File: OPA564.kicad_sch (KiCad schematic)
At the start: 0 parts

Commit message: finished adding all footprints i think
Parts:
- added C1, C11, C4, C6, C7, C9: 0.1 uF, Capacitor_SMD:C_0805_2012Metric_Pad1.18x1.45mm_HandSolder, symbol Device:C
- added C10, C12, C2, C3, C5, C8: 47 uF, Capacitor_SMD:C_1210_3225Metric_Pad1.33x2.70mm_HandSolder, symbol Device:C
- added J1, J2, J4, J5, J6: Conn_Coaxial, 731000154:731000154, symbol Connector:Conn_Coaxial
- added R1, R6, R7: 14.2 kOhms, Resistor_SMD:R_0805_2012Metric_Pad1.20x1.40mm_HandSolder, symbol Device:R_US
- added R2, R3, R4, R5: 1 kOhms, Resistor_SMD:R_0805_2012Metric_Pad1.20x1.40mm_HandSolder, symbol Device:R_US
- added U1, U2, U3: OPA564AIDWPR, OPA564AIDWP:SOIC127P1040X265-21N, symbol 2026-05-25_22-15-10:OPA564AIDWPR
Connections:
- new net: J4.1 (In), U2.15 (VOUT), U2.16 (VOUT), U2.6 (-IN)
- new net: J5.1 (In), R2.2, R3.1, U1.15 (VOUT), U1.16 (VOUT), U2.5 (+IN)
- new net: R6.1, U2.9 (ISET)
- new net: J6.1 (In), R4.2, R5.1, U3.15 (VOUT), U3.16 (VOUT)
- new net: J2.1 (In), U3.5 (+IN)
- new net: R4.1, U3.6 (-IN)
- new net: R7.1, U3.9 (ISET)
- new net: R1.1, U1.9 (ISET)
- new net: J1.1 (In), U1.5 (+IN)
- new net: R2.1, U1.6 (-IN)
- new net +12V: C1.2, C10.2, C2.2, C5.2, C6.2, C9.2, U1.17 (V+PWR), U1.18 (V+PWR), U1.19 (V+PWR), U1.2 (V+), U2.17 (V+PWR), U2.18 (V+PWR), U2.19 (V+PWR), U2.2 (V+), U3.17 (V+PWR), U3.18 (V+PWR), U3.19 (V+PWR), U3.2 (V+)
- new net -12V: C11.1, C12.1, C3.1, C4.1, C7.1, C8.1, R1.2, R6.2, R7.2, U1.1 (V-), U1.10 (V-), U1.11 (V-), U1.13 (V-PWR), U1.14 (V-PWR), U1.20 (V-), U1.21 (EP), U2.1 (V-), U2.10 (V-), U2.11 (V-), U2.13 (V-PWR), U2.14 (V-PWR), U2.20 (V-), U2.21 (EP), U3.1 (V-), U3.10 (V-), U3.11 (V-), U3.13 (V-PWR), U3.14 (V-PWR), U3.20 (V-), U3.21 (EP)
- new net -8V: U1.7 (VDIG), U2.7 (VDIG), U3.7 (VDIG)
- new net GND: C1.1, C10.1, C11.2, C12.2, C2.1, C3.2, C4.2, C5.1, C6.1, C7.2, C8.2, C9.1, J1.2 (Ext), J2.2 (Ext), J4.2 (Ext), J5.2 (Ext), J6.2 (Ext), R3.2, R5.2
- no-connect marks 0 -> 12
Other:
- title: (none) -> OPA564 Function Amplifier

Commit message: Rough Sketch of PCB design has been finished
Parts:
- removed J2, J5: Conn_Coaxial, 731000154:731000154, symbol Connector:Conn_Coaxial
- added J7: V-, bidpl:banana_cinch, symbol Connector:Conn_01x01_Socket
- added J8: V+, bidpl:banana_cinch, symbol Connector:Conn_01x01_Socket
- added J9: GND, bidpl:banana_cinch, symbol Connector:Conn_01x01_Socket
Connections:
- net Signal Input: now reaches U3.5 (+IN)
- net Signal Input: now also J1.1 (In), U1.5 (+IN)
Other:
- moved on the sheet: J1

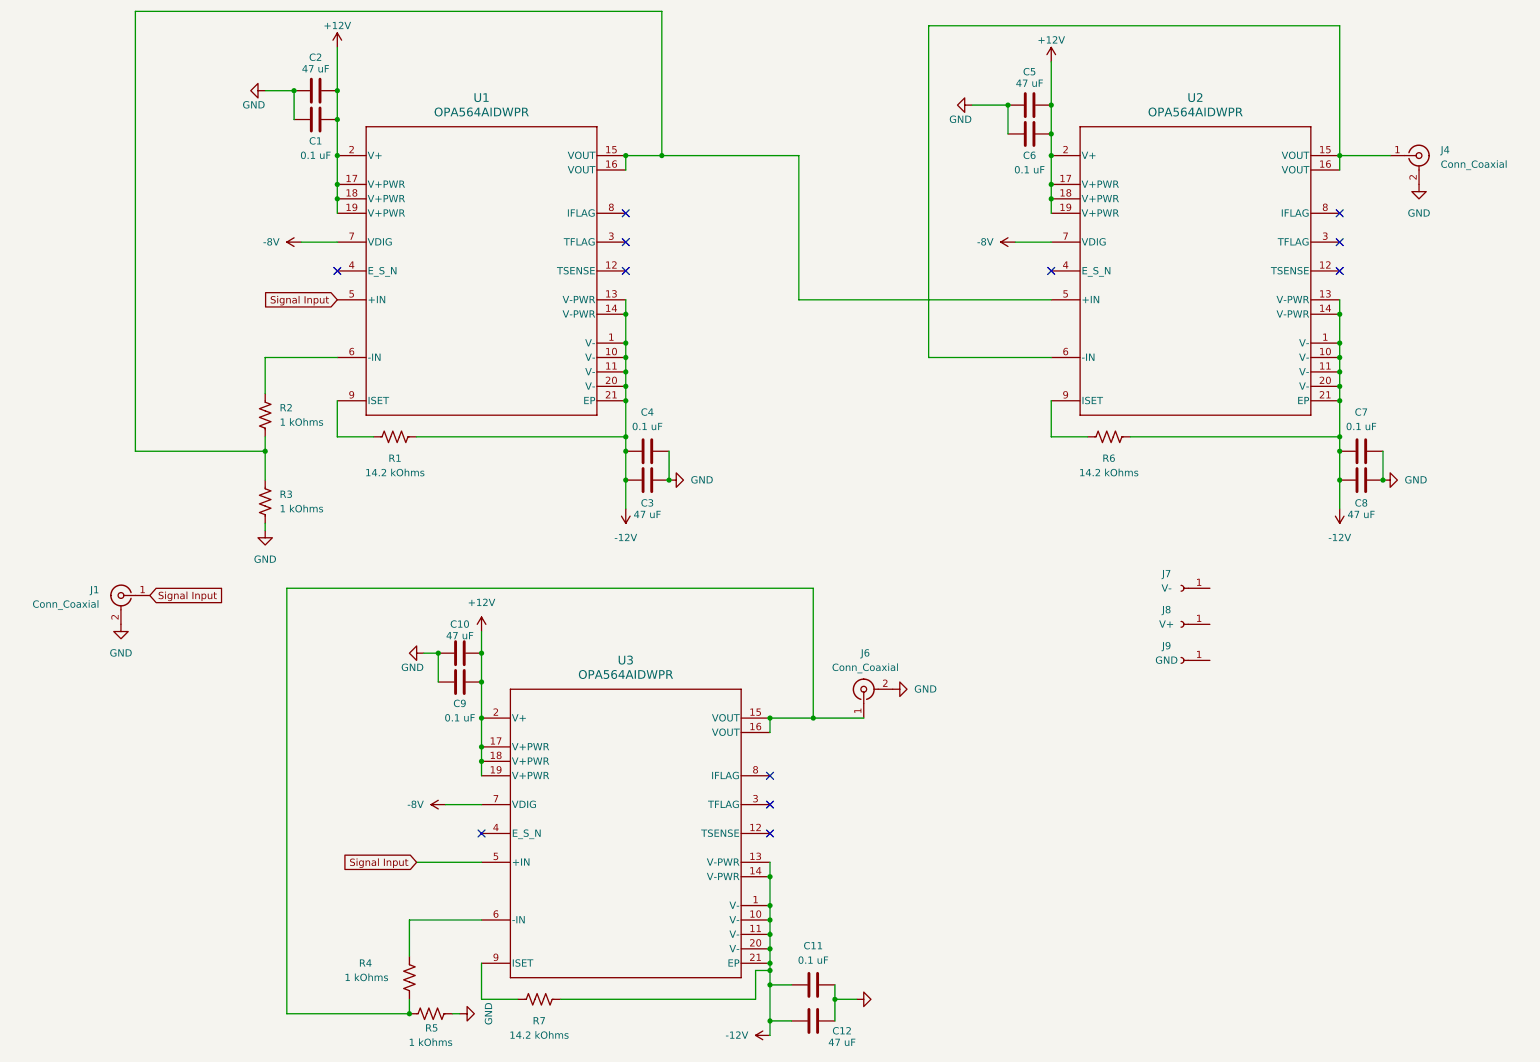
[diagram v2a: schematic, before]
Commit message: OPA564 without Voltage Follower
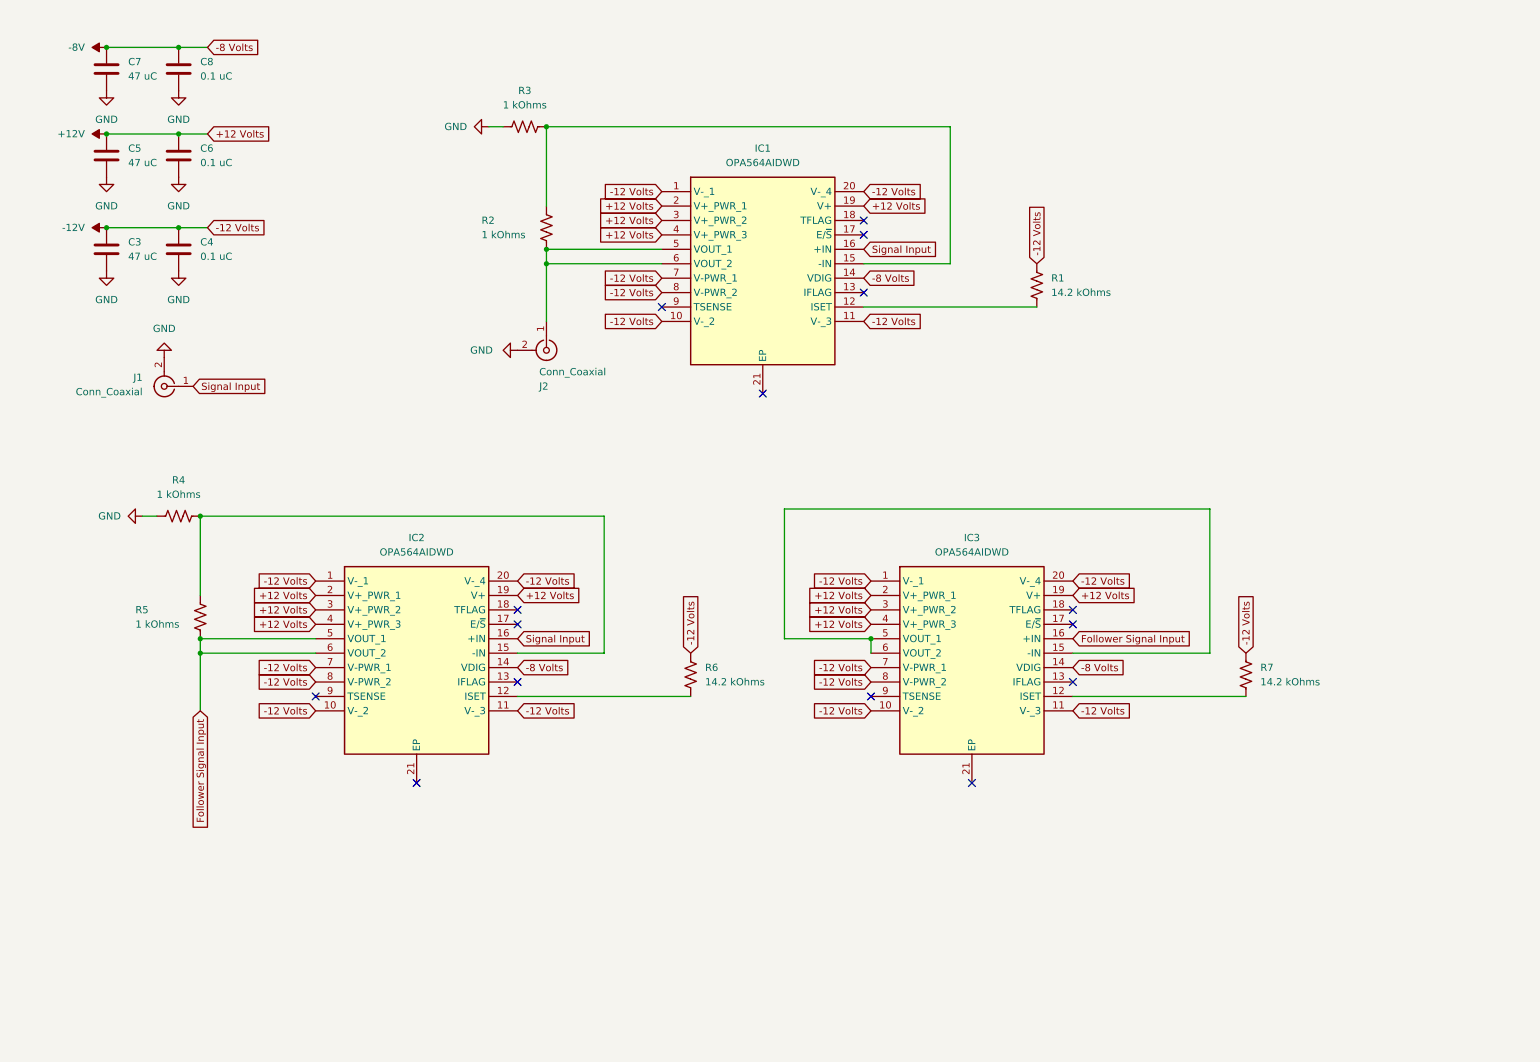
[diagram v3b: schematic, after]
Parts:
- removed C1, C11, C9: 0.1 uF, Capacitor_SMD:C_0805_2012Metric_Pad1.18x1.45mm_HandSolder, symbol Device:C
- removed C10, C12, C2: 47 uF, Capacitor_SMD:C_1210_3225Metric_Pad1.33x2.70mm_HandSolder, symbol Device:C
- removed J4, J6: Conn_Coaxial, 731000154:731000154, symbol Connector:Conn_Coaxial
- removed J7: V-, bidpl:banana_cinch, symbol Connector:Conn_01x01_Socket
- removed J8: V+, bidpl:banana_cinch, symbol Connector:Conn_01x01_Socket
- removed J9: GND, bidpl:banana_cinch, symbol Connector:Conn_01x01_Socket
- removed U1, U2, U3: OPA564AIDWPR, OPA564AIDWP:SOIC127P1040X265-21N, symbol 2026-05-25_22-15-10:OPA564AIDWPR
- added IC1, IC2, IC3: OPA564AIDWD, OPA564AIDWP:SOIC127P1040X265-21N, symbol OPA564AIDWD:OPA564AIDWD
- added J2: Conn_Coaxial, 731000154:731000154, symbol Connector:Conn_Coaxial
- C3, C5: value 47 uF -> 47 uC; footprint Capacitor_SMD:C_1210_3225Metric_Pad1.33x2.70mm_HandSolder -> Capacitor_SMD:C_1812_4532Metric_Pad1.57x3.40mm_HandSolder
- C4, C6: value 0.1 uF -> 0.1 uC
- C7: value 0.1 uF -> 47 uC; footprint Capacitor_SMD:C_0805_2012Metric_Pad1.18x1.45mm_HandSolder -> Capacitor_SMD:C_1812_4532Metric_Pad1.57x3.40mm_HandSolder
- C8: value 47 uF -> 0.1 uC; footprint Capacitor_SMD:C_1210_3225Metric_Pad1.33x2.70mm_HandSolder -> Capacitor_SMD:C_0805_2012Metric_Pad1.18x1.45mm_HandSolder
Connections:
- net +12V: now also IC1.19 (V+), IC1.2 (V+_PWR_1), IC1.3 (V+_PWR_2), IC1.4 (V+_PWR_3), IC2.19 (V+), IC2.2 (V+_PWR_1), IC2.3 (V+_PWR_2), IC2.4 (V+_PWR_3), IC3.19 (V+), IC3.2 (V+_PWR_1), IC3.3 (V+_PWR_2), IC3.4 (V+_PWR_3)
- net -12V: now also C3.2, C4.2, R1.1, R6.1, R7.1, IC1.1 (V-_1), IC1.10 (V-_2), IC1.11 (V-_3), IC1.20 (V-_4), IC1.7 (V-PWR_1), IC1.8 (V-PWR_2), IC2.1 (V-_1), IC2.10 (V-_2), IC2.11 (V-_3), IC2.20 (V-_4), IC2.7 (V-PWR_1), IC2.8 (V-PWR_2), IC3.1 (V-_1), IC3.10 (V-_2), IC3.11 (V-_3), IC3.20 (V-_4), IC3.7 (V-PWR_1), IC3.8 (V-PWR_2); no longer C3.1, C4.1, C7.1, C8.1, R1.2, R6.2, R7.2
- net -8V: now also C7.2, C8.2, IC1.14 (VDIG), IC2.14 (VDIG), IC3.14 (VDIG)
- net GND: now also C3.1, C4.1, C7.1, C8.1, R3.1, R4.1, J2.2 (Ext); no longer C3.2, C4.2, C7.2, C8.2, R3.2, R5.2
- net Signal Input: now also IC1.16 (+IN), IC2.16 (+IN)
- net at R2.2: now also IC1.5 (VOUT_1), IC1.6 (VOUT_2), J2.1 (In); no longer R3.1
- net at R4.2, R5.1: now also IC2.15 (-IN)
- net at R2.1: now also R3.2, IC1.15 (-IN)
- new net: IC3.12 (ISET), R7.2
- new net: IC3.15 (-IN), IC3.5 (VOUT_1), IC3.6 (VOUT_2)
- new net: IC1.12 (ISET), R1.2
- new net: IC2.12 (ISET), R6.2
- new net Follower Signal Input: IC2.5 (VOUT_1), IC2.6 (VOUT_2), IC3.16 (+IN), R5.2
- no-connect marks 12 -> 15

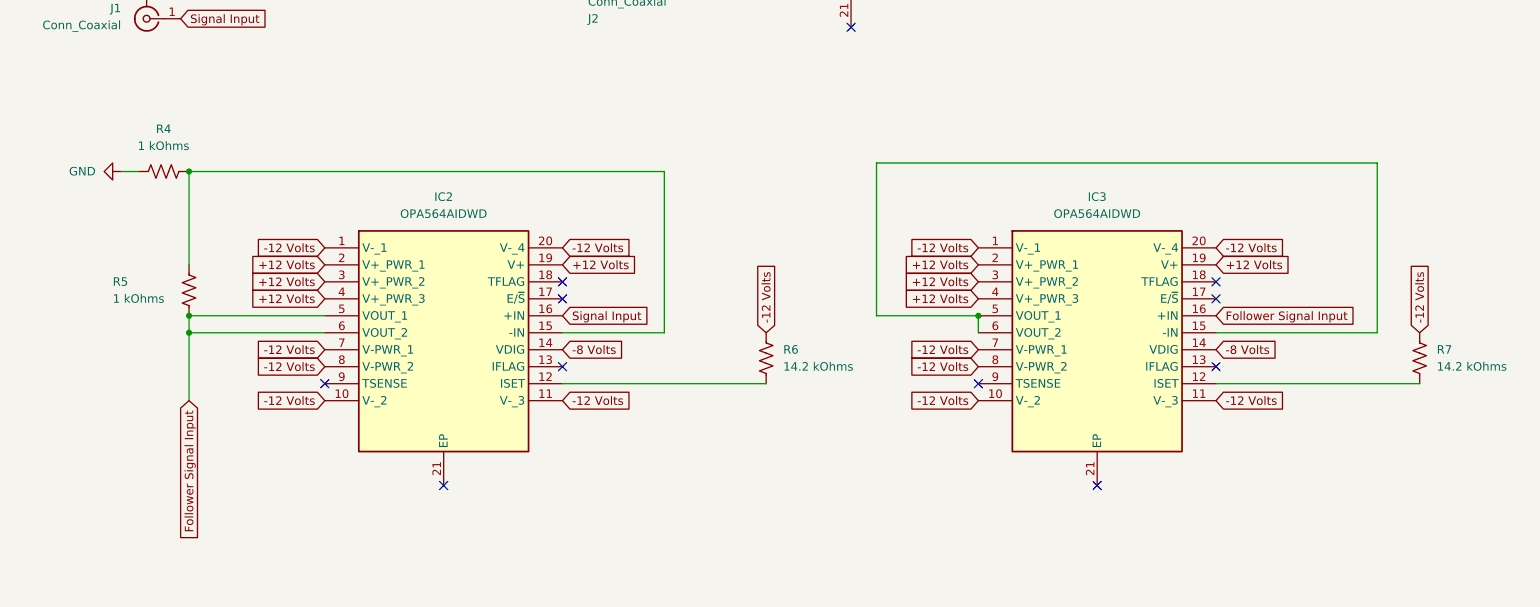
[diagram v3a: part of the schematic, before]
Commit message: OPA564 without voltage follower
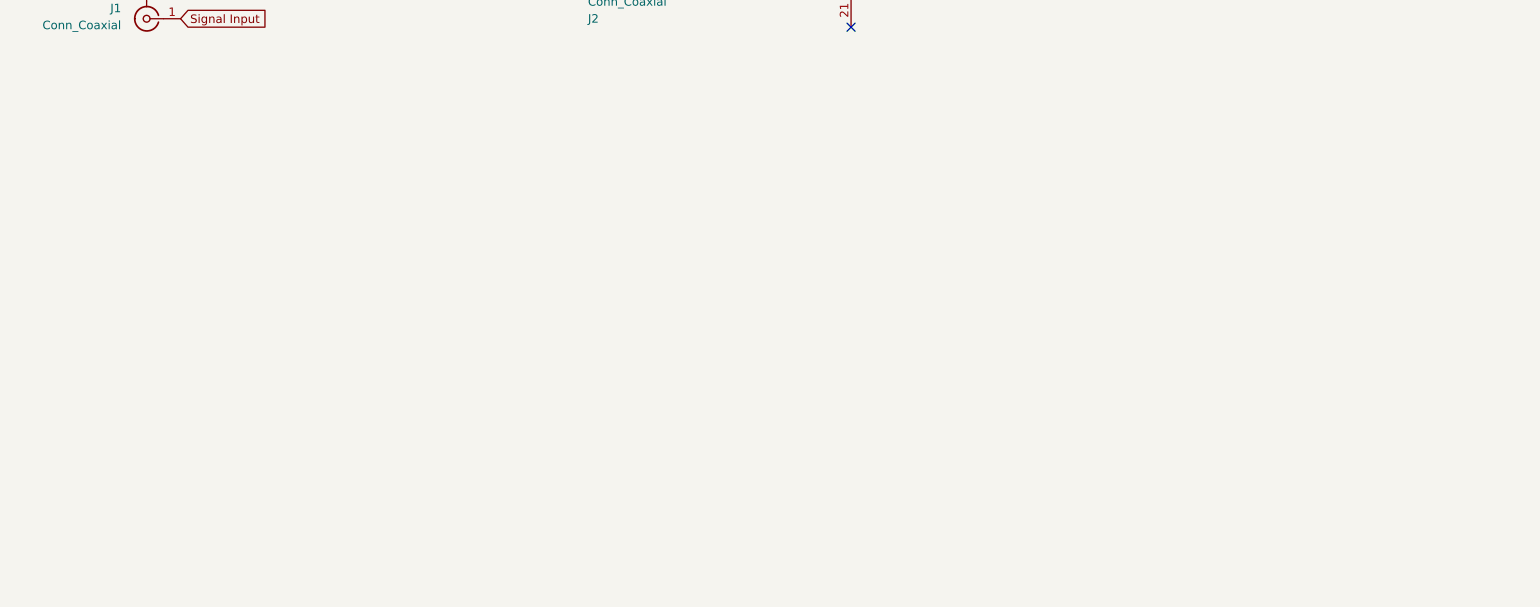
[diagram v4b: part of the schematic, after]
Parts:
- removed IC2, IC3: OPA564AIDWD, OPA564AIDWP:SOIC127P1040X265-21N, symbol OPA564AIDWD:OPA564AIDWD
- removed R4, R5: 1 kOhms, Resistor_SMD:R_0805_2012Metric_Pad1.20x1.40mm_HandSolder, symbol Device:R_US
- removed R6, R7: 14.2 kOhms, Resistor_SMD:R_0805_2012Metric_Pad1.20x1.40mm_HandSolder, symbol Device:R_US
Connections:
- no-connect marks 15 -> 5

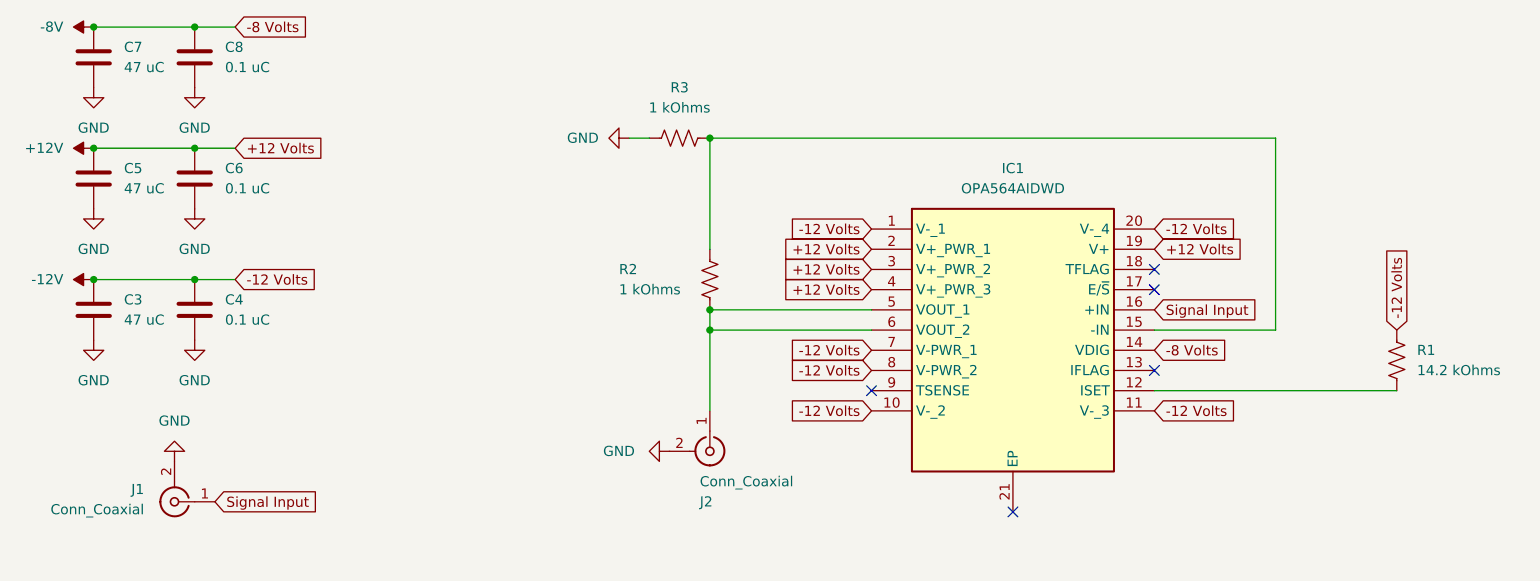
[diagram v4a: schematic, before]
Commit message: OPA564 simplest design
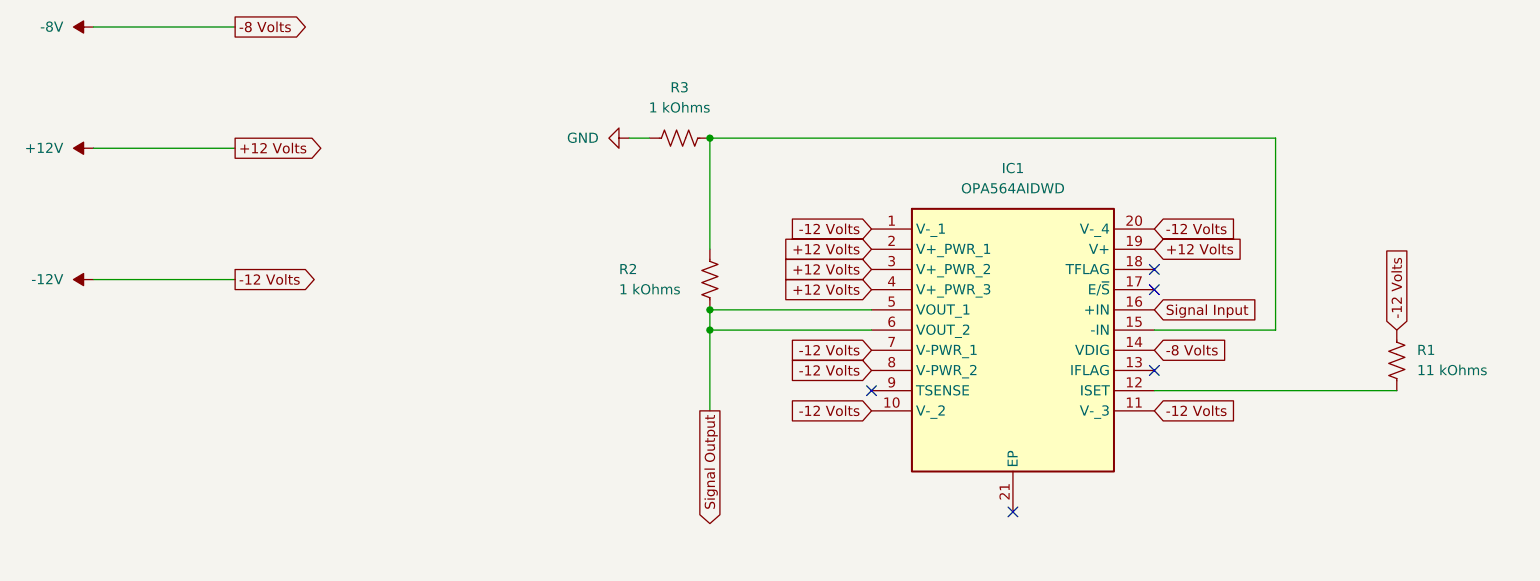
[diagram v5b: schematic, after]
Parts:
- removed C3, C5, C7: 47 uC, Capacitor_SMD:C_1812_4532Metric_Pad1.57x3.40mm_HandSolder, symbol Device:C
- removed C4, C6, C8: 0.1 uC, Capacitor_SMD:C_0805_2012Metric_Pad1.18x1.45mm_HandSolder, symbol Device:C
- removed J1, J2: Conn_Coaxial, 731000154:731000154, symbol Connector:Conn_Coaxial
- R1: value 14.2 kOhms -> 11 kOhms
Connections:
- net Signal Output: now reaches IC1.5 (VOUT_1), IC1.6 (VOUT_2), R2.2
